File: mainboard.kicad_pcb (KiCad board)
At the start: 2 copper layers, 39 parts, among them J1 DRV8833-1, J10 Conn_02x04_Counter_Clockwise, J11 Conn_02x04_Counter_Clockwise, J12 Conn_02x04_Counter_Clockwise, J2 DRV8833-0, J3 Conn_01x02, J4 Screw_Terminal_01x06, J5 Screw_Terminal_01x06, J6 VIM4_HEADER, J7 Conn_01x02, J8 Conn_01x02, J9 Conn_02x04_Counter_Clockwise, Q1 2N7000, Q2 2N7000, SW1 RotaryEncoder_Switch, U1 MCP23017_SP

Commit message: General reorganization
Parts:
- moved R9 220.4 mm to (267.6, 60.5)
- moved C1 151.0 mm to (72.5, 84.5)
- moved C2 151.0 mm to (72.5, 87.5)
- moved RN1 91.9 mm to (135.5, 65.0), turned to 180 degrees
- moved J6 79.1 mm to (95.9, 88.0), turned to 90 degrees
- moved Brd1 44.8 mm to (87.0, 68.9), turned to -90 degrees
- moved SW1 34.9 mm to (54.5, 57.1)

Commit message: Settings import
Imported settings for traces and routing,
Placing and organizing PCB components into modules
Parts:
- removed the J9 at (205.7, 21.5)
- added J12: Conn_02x04_Counter_Clockwise, Connector_PinHeader_2.54mm:PinHeader_2x04_P2.54mm_Vertical, F.Cu at (110.5, 193.0)
- moved J9 263.8 mm to (26.7, 193.0), turned to 90 degrees
- moved J10 233.4 mm to (54.6, 193.0), turned to 90 degrees
- moved J11 219.8 mm to (82.5, 193.0), turned to 90 degrees
- moved F4 208.1 mm to (27.9, 160.4), turned to 90 degrees
- moved F3 187.9 mm to (55.9, 160.4), turned to 90 degrees
- moved F1 172.5 mm to (86.4, 159.9), turned to 90 degrees
- moved F2 150.3 mm to (111.8, 159.9), turned to 90 degrees
- moved Q1 138.0 mm to (124.5, 151.1)
- moved Q2 131.9 mm to (124.5, 143.5)
- moved J7 127.0 mm to (130.8, 153.7), turned to 180 degrees
- moved J8 126.7 mm to (130.8, 146.1), turned to 180 degrees
- moved R1 124.5 mm to (125.7, 154.9), turned to -90 degrees
- moved R2 120.2 mm to (130.8, 157.8), turned to 90 degrees
- moved R3 115.0 mm to (134.6, 157.1), turned to 90 degrees
- moved C3 110.5 mm to (128.3, 157.8), turned to 90 degrees
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- renumbered J12 to J9
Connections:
- F1 pad 1: Net-(J9-Pin_1) -> Net-(J11-Pin_7)
- F2 pad 1: Net-(J10-Pin_1) -> Net-(J12-Pin_7)
- F3 pad 1: Net-(J11-Pin_1) -> Net-(J10-Pin_7)
- F4 pad 1: Net-(J12-Pin_1) -> Net-(J9-Pin_7)
- J1 pad 3: 12V -> 12V_BUCK
- J10 pad 1: Net-(J10-Pin_1) -> MAINS
- J10 pad 2: GND -> MAINS
- J10 pad 4: MAINS -> GND
- J10 pad 5: MAINS -> GND
- J10 pad 7: GND -> Net-(J10-Pin_7)
- J10 pad 8: Net-(J10-Pin_1) -> Net-(J10-Pin_7)
- J11 pad 1: Net-(J11-Pin_1) -> MAINS
- J11 pad 2: GND -> MAINS
- J11 pad 4: MAINS -> GND
- J11 pad 5: MAINS -> GND
- J11 pad 7: GND -> Net-(J11-Pin_7)
- J11 pad 8: Net-(J11-Pin_1) -> Net-(J11-Pin_7)
- J2 pad 3: 12V -> 12V_BUCK
- J9 pad 1: Net-(J12-Pin_1) -> MAINS
- J9 pad 2: GND -> MAINS
- J9 pad 4: MAINS -> GND
- J9 pad 5: MAINS -> GND
- J9 pad 7: GND -> Net-(J9-Pin_7)
- J9 pad 8: Net-(J12-Pin_1) -> Net-(J9-Pin_7)
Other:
- board text added: "12V"
- board text added: "3V"
- board text added: "5V"
- board text added: "9V"
- board text added: "HEADLIGHTS"

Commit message: Circuit adjustments / PCB component Grouping
Removed resistor on LDR in schem. Changed to 10k resistor. Added hole distance for PCA9685, SSD1309.  Grouped components.  Awaiting PIC_FOR_ADC from Dustin
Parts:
- removed R8: 47k, Resistor_SMD:R_0805_2012Metric
- added J13: Conn_01x06, Connector_JST:JST_EH_B6B-EH-A_1x06_P2.50mm_Vertical, F.Cu at (81.3, 30.3)
- R10: value 1k -> 10k
- moved R4 158.6 mm to (76.6, 88.9)
- moved R5 158.6 mm to (76.6, 91.8)
- moved R9 157.2 mm to (115.6, 100.3)
- moved F2 136.5 mm to (19.1, 59.7), turned to 0 degrees
- moved C6 129.4 mm to (115.2, 107.6), turned to -90 degrees
- moved R6 127.2 mm to (138.4, 106.3), turned to -90 degrees
- moved J3 126.1 mm to (142.2, 101.6)
- moved R7 124.1 mm to (142.2, 108.9), turned to -90 degrees
- moved R10 121.4 mm to (119.0, 107.6), turned to 90 degrees
- moved C3 121.2 mm to (26.7, 91.8)
- moved R1 121.2 mm to (24.1, 88.9)
- moved C4 121.2 mm to (34.0, 80.0)
- moved J7 121.2 mm to (29.2, 87.6)
- moved J8 121.2 mm to (29.2, 80.0)
- moved Q1 121.2 mm to (22.9, 85.1)
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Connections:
- Brd1 pad 2: 3v3 -> PICO_3V3
- C6 pad 1: ADC_SIG -> Net-(C6-Pad1)
- J6 pad 32: unconnected-(J6-Pin_32-Pad32) -> PIC_ADC
- R10 pad 1: Net-(R10-Pad1) -> ADC_SIG
- R10 pad 2: ADC_SIG -> Net-(C6-Pad1)
- R9 pad 2: Net-(R10-Pad1) -> ADC_SIG
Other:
- board text added: "3.3V"
- board text added: "Conn_02x04_Counter_Clockwise"
- board text added: "DISPLAY"
- board text added: "LDR"
- board text added: "PCA9685"
- board text added: "SWITCH/BUTTON FILTER"
- board text removed: "3V"

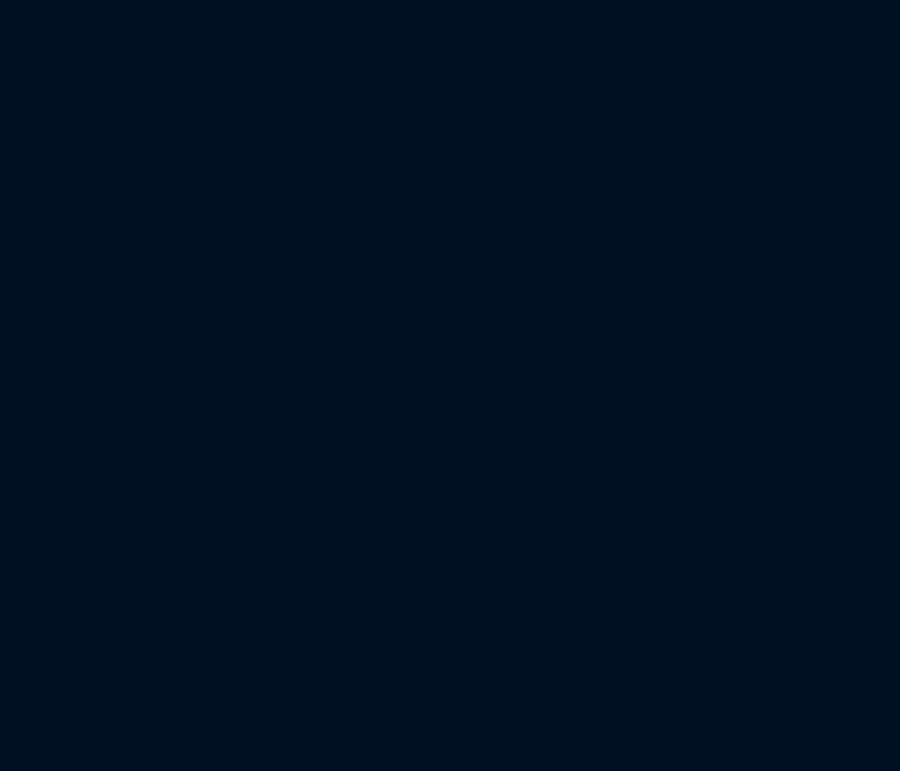
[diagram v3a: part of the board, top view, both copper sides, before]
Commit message: PIC16F819-ISO Added
Added PIC, changed footprint to match our 18pin SMD.

LDR circuit and connection to VIM4 need to be made
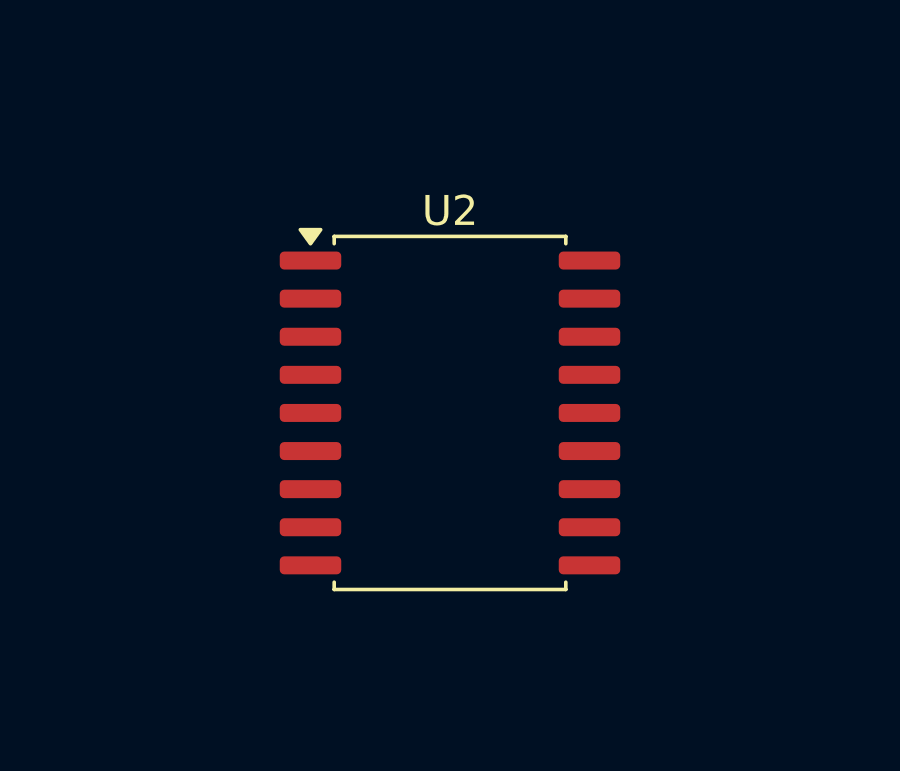
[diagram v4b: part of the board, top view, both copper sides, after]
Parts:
- added U2: PIC16F819-ISO, Package_SO:SOIC-18W_7.5x11.6mm_P1.27mm, F.Cu at (120.0, 65.5)

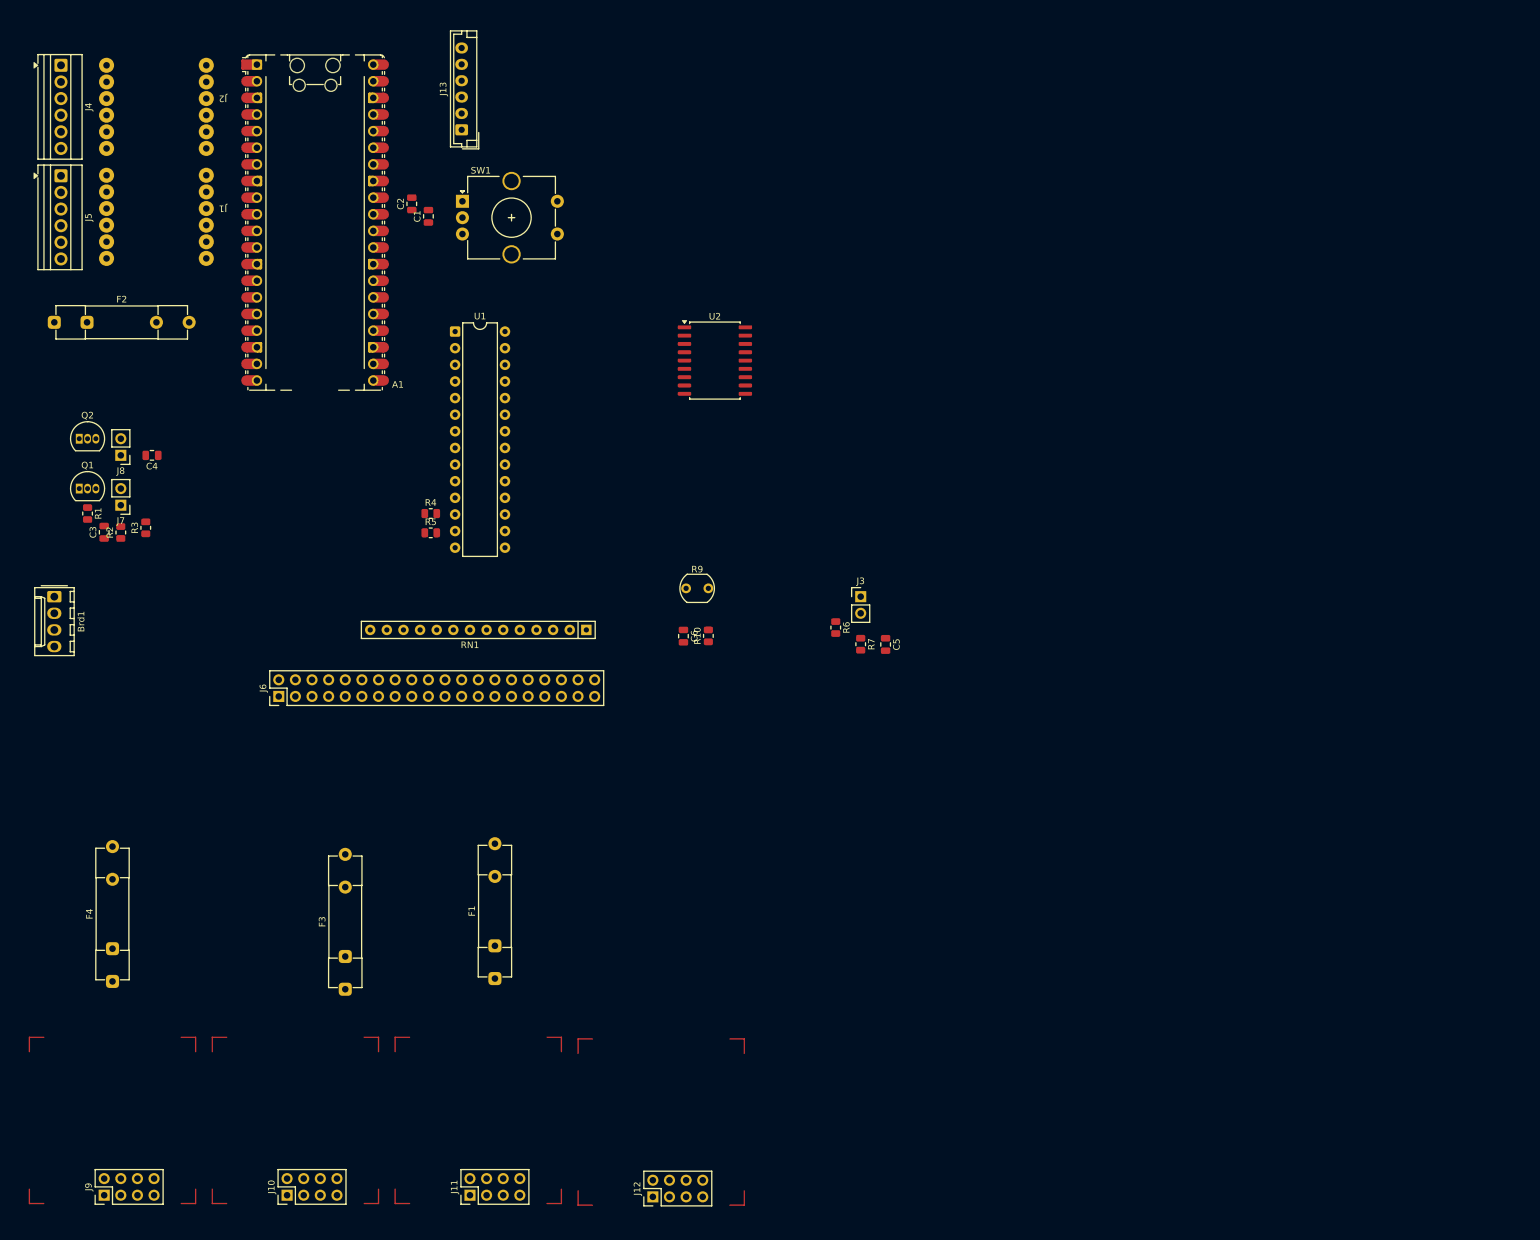
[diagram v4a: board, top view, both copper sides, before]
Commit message: Rearrangement and first pour
Modified the order of operations for terminal block to fuse to buck. Added a few things like the holes for the Roboclaws, removed the display, since we're going to wire it using a JST connector in order for it to exist somewhere else on the robot.  I added a PIC footprint that fits the PIC16F819-ISO, and generally hooked it up.

I still need to check with Dustin and make sure that the VIM4 connection to the PIC is the one we want to use.

I also need to know the exact dimensions of the PCB constraint we are designing this for.
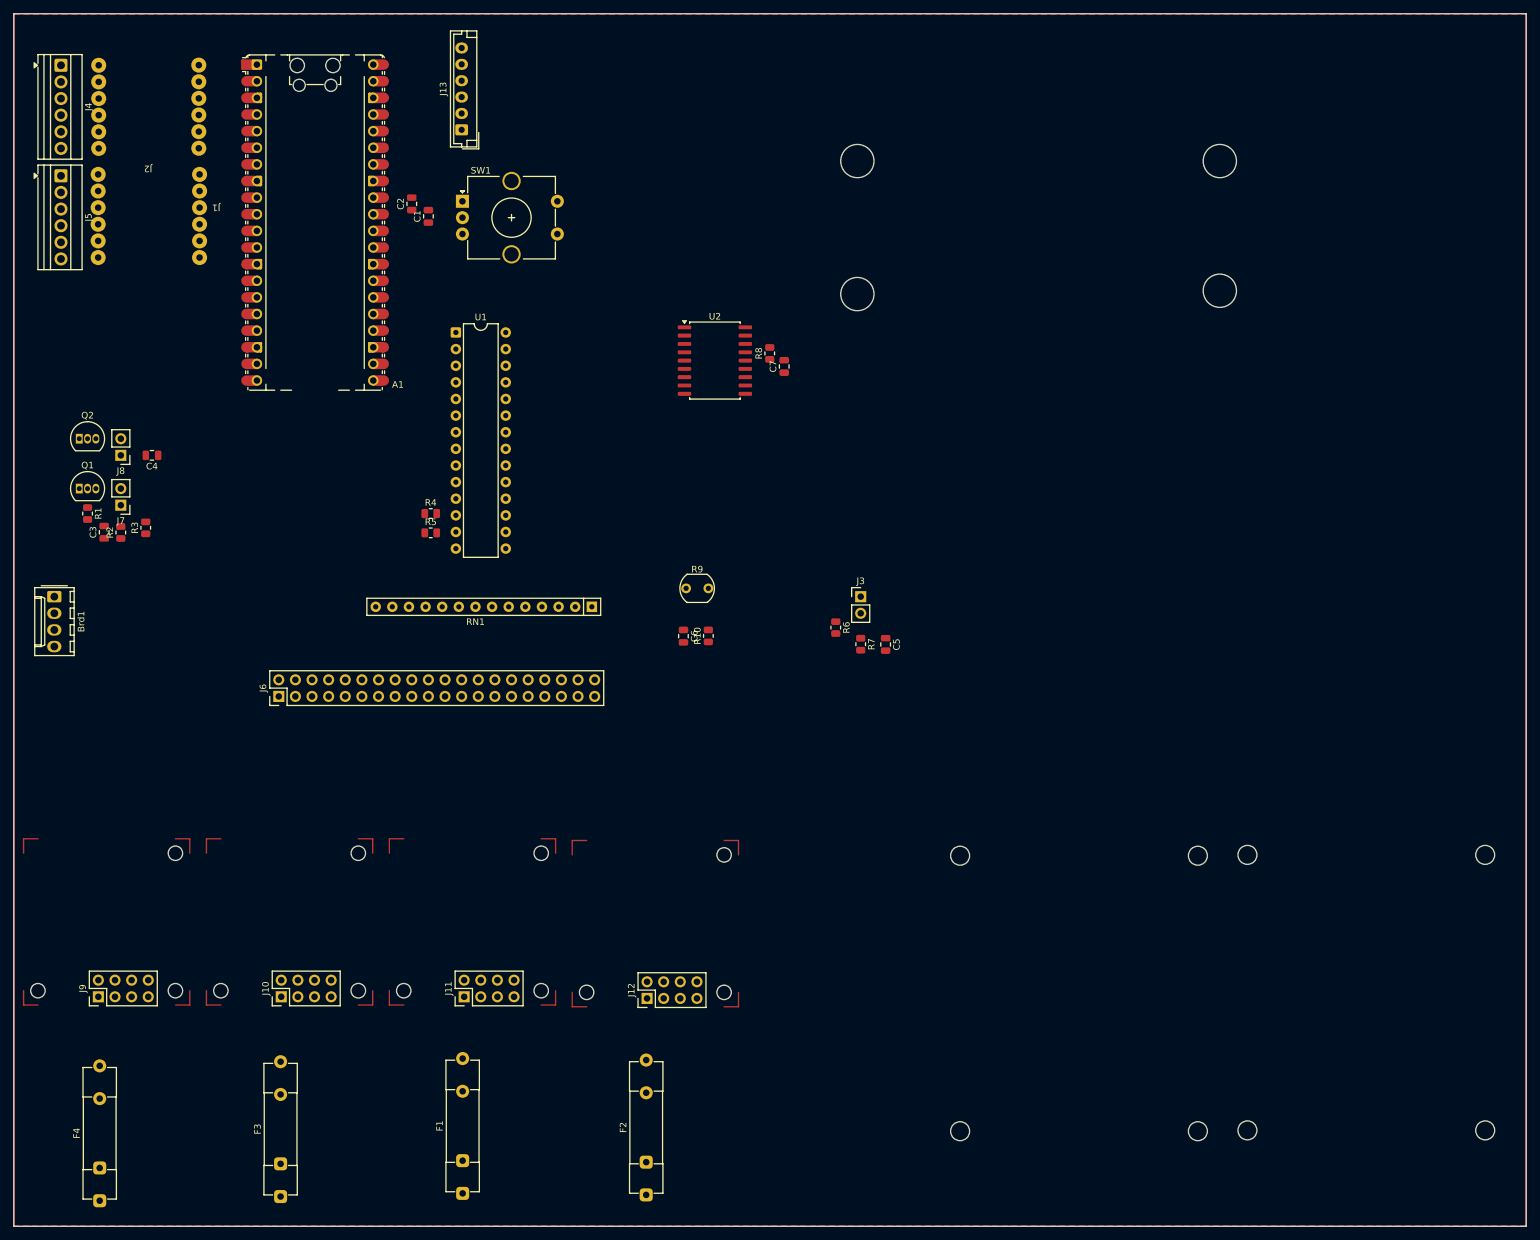
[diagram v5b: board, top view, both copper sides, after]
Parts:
- added C7: 0.1uF, Capacitor_SMD:C_0805_2012Metric, F.Cu at (130.6, 66.4)
- added R8: 10k, Resistor_SMD:R_0805_2012Metric, F.Cu at (128.3, 64.4)
- moved F2 161.1 mm to (109.5, 193.0), turned to 90 degrees
- moved F4 33.6 mm to (26.0, 193.9)
- moved F1 33.2 mm to (81.4, 192.8)
- moved F3 33.2 mm to (53.6, 193.2)
- moved J10 30.3 mm to (53.7, 162.7)
- moved J11 30.3 mm to (81.7, 162.7)
- moved J12 30.3 mm to (109.6, 163.0)
- moved J9 30.3 mm to (25.8, 162.7)
- moved RN1 3.63 mm to (101.2, 103.1)
- moved J1 1.79 mm to (42.8, 35.5)
- moved J2 1.65 mm to (42.7, 18.8)
- moved U1 0.18 mm to (80.4, 61.2)
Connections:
- F1 pad 1: Net-(J11-Pin_7) -> MAIN_BUS
- F1 pad 2: 9V_BUCK -> Net-(J11-Pin_1)
- F2 pad 1: Net-(J12-Pin_7) -> MAIN_BUS
- F2 pad 2: 12V_BUCK -> Net-(J12-Pin_1)
- F3 pad 1: Net-(J10-Pin_7) -> MAIN_BUS
- F3 pad 2: 5V_BUCK -> Net-(J10-Pin_1)
- F4 pad 1: Net-(J9-Pin_7) -> MAIN_BUS
- F4 pad 2: 3V_BUCK -> Net-(J9-Pin_1)
- J10 pad 1: MAINS -> Net-(J10-Pin_1)
- J10 pad 2: MAINS -> Net-(J10-Pin_1)
- J10 pad 7: Net-(J10-Pin_7) -> 5V_BUCK
- J10 pad 8: Net-(J10-Pin_7) -> 5V_BUCK
- J11 pad 1: MAINS -> Net-(J11-Pin_1)
- J11 pad 2: MAINS -> Net-(J11-Pin_1)
- J11 pad 7: Net-(J11-Pin_7) -> 9V_BUCK
- J11 pad 8: Net-(J11-Pin_7) -> 9V_BUCK
- J12 pad 1: MAINS -> Net-(J12-Pin_1)
- J12 pad 2: MAINS -> Net-(J12-Pin_1)
- J12 pad 7: Net-(J12-Pin_7) -> 12V_BUCK
- J12 pad 8: Net-(J12-Pin_7) -> 12V_BUCK
- J6 pad 32: PIC_ADC -> PIC_STATE
- J9 pad 1: MAINS -> Net-(J9-Pin_1)
- J9 pad 2: MAINS -> Net-(J9-Pin_1)
- J9 pad 7: Net-(J9-Pin_7) -> 3V_BUCK
- J9 pad 8: Net-(J9-Pin_7) -> 3V_BUCK
- R10 pad 1: ADC_SIG -> LDR_ADC
- R9 pad 2: ADC_SIG -> LDR_ADC
- U2 pad 14: unconnected-(U2-VDD-Pad14) -> 3V_BUCK
- U2 pad 17: unconnected-(U2-AN0/RA0-Pad17) -> LDR_ADC
- U2 pad 3: unconnected-(U2-T0CKL/AN4/RA4-Pad3) -> PIC_STATE
- U2 pad 4: unconnected-(U2-Vpp/~{MCLR}/RA5-Pad4) -> Net-(U2-Vpp/~{MCLR}/RA5)
- U2 pad 5: unconnected-(U2-VSS-Pad5) -> GND
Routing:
- added copper zone on B.Cu, net GND
- added copper zone on F.Cu, net GND
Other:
- board outline added: 231.1 x 185.2 mm
- board text added: "ROBOCLAW"
- board text removed: "DISPLAY"
